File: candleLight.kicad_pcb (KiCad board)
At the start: 2 copper layers, 46.4 x 20 mm, 45 parts, among them J1 USB_C_Receptacle_USB2.0, J2 Conn_Phoenix, J3 Conn_SWD, J4 Conn_3.3V, U1 ME6210A33PG, U2 STM32F072C8Tx, U3 TJA1051/3, Y1 8MHz

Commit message: inital board
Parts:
- removed J4: Conn_3.3V, Connector_PinHeader_2.54mm:PinHeader_1x02_P2.54mm_Vertical
- removed R1, R2: 4K7, Resistor_SMD:R_0603_1608Metric
- removed SCL1: SCL1, Measurement_Points:Measurement_Point_Round-SMD-Pad_Small
- removed SDA1: SDA1, Measurement_Points:Measurement_Point_Round-SMD-Pad_Small
- removed W1, W2: TEST_1P, Measurement_Points:Measurement_Point_Round-SMD-Pad_Big
- removed W3, W4, W5, W6, W7, W8: TEST_1P, Measurement_Points:Measurement_Point_Round-SMD-Pad_Small
- added C13: 100nF, Capacitor_SMD:C_0603_1608Metric, F.Cu at (136.2, 77.0)
- added C14: 100nF, Capacitor_SMD:C_0603_1608Metric, F.Cu at (149.0, 71.0)
- added C15: 10uF, Capacitor_SMD:C_0805_2012Metric, F.Cu at (149.0, 69.0)
- added SW1: TS-1088R-02526, stm32world:TS-1088R-02526, F.Cu at (164.1, 88.0)
- added SW2: TS-1088R-02526, stm32world:TS-1088R-02526, F.Cu at (164.1, 84.0)
- added SW3: MST22D18G2 125, woldhack:SW-SMD_MST22D18G2, F.Cu at (130.4, 85.8)
- C1, C2: value 10uF -> 30pF; footprint Capacitor_SMD:C_0805_2012Metric -> Capacitor_SMD:C_0603_1608Metric
- C10: value 10uF -> 100nF; footprint Capacitor_SMD:C_0805_2012Metric -> Capacitor_SMD:C_0603_1608Metric
- C12, C5: value 100nF -> 10uF; footprint Capacitor_SMD:C_0603_1608Metric -> Capacitor_SMD:C_0805_2012Metric
- C3: value 30pF -> 100nF
- C4: value 30pF -> 10uF; footprint Capacitor_SMD:C_0603_1608Metric -> Capacitor_SMD:C_0805_2012Metric
- J3: value Conn_SWD -> Conn_01x05; footprint Connector_PinHeader_2.54mm:PinHeader_1x03_P2.54mm_Vertical -> Connector_PinHeader_2.54mm:PinHeader_1x05_P2.54mm_Vertical
- R11: value 5k1 -> 1K
- R3: value dnp -> 5k1; footprint Resistor_SMD:R_0805_2012Metric -> Resistor_SMD:R_0603_1608Metric
- R4: value 1K -> 5k1
- R5: value 5k1 -> 10K
- R7: value dnp -> 10K; footprint Resistor_SMD:R_0805_2012Metric -> Resistor_SMD:R_0603_1608Metric
- R8: value 1K -> 120
- U1: value ME6210A33PG -> STM32F072C8Tx; footprint Package_TO_SOT_SMD:SOT-89-3 -> Package_QFP:LQFP-48_7x7mm_P0.5mm
- U2: value STM32F072C8Tx -> ME6210A33PG; footprint Package_QFP:LQFP-48_7x7mm_P0.5mm -> Package_TO_SOT_SMD:SOT-89-3
- moved J1 125.0 mm to (168.8, 75.5), turned to 90 degrees
- moved J3 113.8 mm to (157.7, 65.0), turned to 90 degrees
- moved G*** 111.6 mm to (173.5, 43.5)
- moved R4 104.8 mm to (158.8, 73.8), turned to 180 degrees
- moved R5 103.6 mm to (152.6, 86.0)
- moved R3 102.4 mm to (158.8, 76.8), turned to 0 degrees
- moved U2 100.7 mm to (158.0, 85.5), turned to -90 degrees
- moved R11 96.7 mm to (143.9, 88.3)
- moved C4 94.2 mm to (158.9, 81.7), turned to 0 degrees
- moved R10 92.0 mm to (146.9, 88.3), turned to 90 degrees
- moved C7 89.6 mm to (138.5, 71.0)
- moved C5 89.6 mm to (154.4, 82.6), turned to 90 degrees
- moved D3 89.1 mm to (142.4, 88.3), turned to -90 degrees
- moved D2 88.9 mm to (145.4, 88.3), turned to -90 degrees
- moved C10 85.6 mm to (146.0, 81.8), turned to 180 degrees
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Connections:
- C1 pad 1: +5V -> GND
- C1 pad 2: GND -> Net-(U1-PF0)
- C11 pad 1: +5V -> +3V3
- C2 pad 1: +3V3 -> GND
- C2 pad 2: GND -> Net-(U1-PF1)
- C3 pad 1: GND -> NRST
- C3 pad 2: Net-(U2-PF0) -> GND
- C4 pad 1: GND -> +5V
- C4 pad 2: Net-(U2-PF1) -> GND
- C5 pad 1: NRST -> +3V3
- C6 pad 1: +3V3 -> +5V
- J3 pad 1: NRST -> +3V3
- J3 pad 2: SWCLK -> NRST
- J3 pad 3: SWDIO -> SWCLK
- R10 pad 1: Net-(D3-A) -> Net-(D2-A)
- R11 pad 1: Net-(J1-CC2) -> Net-(D3-A)
- R11 pad 2: GND -> +3V3
- R3 pad 1: +3V3 -> GND
- R3 pad 2: Net-(U2-BOOT0) -> Net-(J1-CC1)
- R4 pad 1: GND -> Net-(J1-CC2)
- R4 pad 2: Net-(U2-BOOT0) -> GND
- R5 pad 1: GND -> +3V3
- R5 pad 2: Net-(J1-CC1) -> NRST
- R7 pad 1: CAN_H -> BO0
- R7 pad 2: CAN_L -> GND
- R8 pad 1: Net-(D1-A) -> Net-(R8-Pad1)
- R8 pad 2: +3V3 -> CAN_L
- R9 pad 1: Net-(D2-A) -> Net-(D1-A)
- U1 pad 1: GND -> +3V3
- U1 pad 2: +5V -> CAN_S
- U1 pad 3: +3V3 -> unconnected-(U1-PC14-Pad3)
- U2 pad 1: +3V3 -> GND
- U2 pad 2: CAN_S -> +5V
- U2 pad 3: unconnected-(U2-PC14-Pad3) -> +3V3
- Y1 pad 1: Net-(U2-PF0) -> Net-(U1-PF0)
- Y1 pad 2: Net-(U2-PF1) -> Net-(U1-PF1)
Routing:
- net +3V3: track 7.37 -> 135.0 mm, vias 4 -> 8
- net NRST: track 20.2 -> 66.5 mm, vias 3 -> 4
- net BO0: track 0.00 -> 31.2 mm, vias 0 -> 3
- net GND: track 38.6 -> 10.8 mm
- net +5V: track 66.5 -> 52.8 mm, vias 5 -> 2
- net CAN_L: track 18.5 -> 30.9 mm
- net USB_DN: track 8.20 -> 20.1 mm
- net USB_DP: track 8.18 -> 20.1 mm
- net Net-(U1-PF0): track 0.00 -> 11.0 mm
- net CAN_H: track 20.2 -> 30.8 mm
- net Net-(U1-PF1): track 0.00 -> 9.83 mm
- net Net-(U2-PF1): track 9.24 -> 0.00 mm
- net Net-(U2-PB6): track 8.98 -> 0.00 mm, vias 1 -> 0
- net Net-(U2-PF0): track 8.31 -> 0.00 mm
- net Net-(U2-PB7): track 7.74 -> 0.00 mm, vias 1 -> 0
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- added copper zone on F.Cu, net GND
- removed copper zone on F.Cu, net +3V3
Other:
- board size 46.4 x 20 mm -> 59 x 29.6 mm
- board text removed: "+5V"
- board text removed: "3V3"
- board text removed: "B"
- board text removed: "CAN_H"
- board text removed: "CAN_L"
- board text removed: "CLK"
- board text removed: "CS"
- board text removed: "GND"
- board text removed: "IO"
- board text removed: "MISO"
- board text removed: "MOSI"
- board text removed: "PWR"
- board text removed: "RST"
- board text removed: "RX"
- board text removed: "SCK"
- board text removed: "SCL"
- board text removed: "SDA"
- board text removed: "T"
- board text removed: "TX"

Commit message: layout
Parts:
- removed C15: 10uF, Capacitor_SMD:C_0805_2012Metric
- removed R10, R11: 1K, Resistor_SMD:R_0603_1608Metric
- removed SW2: TS-1088R-02526, stm32world:TS-1088R-02526
- removed SW3: MST22D18G2 125, woldhack:SW-SMD_MST22D18G2
- added D4: PSM712, Package_TO_SOT_SMD:SOT-23, F.Cu at (158.5, 75.2)
- added D5: ~, Diode_SMD:D_SOD-123, F.Cu at (166.8, 82.5)
- added H1: MountingHole, MountingHole:MountingHole_2.1mm, F.Cu at (117.0, 63.8)
- added H2: MountingHole, MountingHole:MountingHole_2.1mm, F.Cu at (170.0, 63.8)
- added H3: MountingHole, MountingHole:MountingHole_2.1mm, F.Cu at (170.0, 87.2)
- added H4: MountingHole, MountingHole:MountingHole_2.1mm, F.Cu at (117.0, 87.2)
- added J4: Conn_USART1, Connector_PinHeader_2.54mm:PinHeader_1x02_P2.54mm_Vertical, F.Cu at (148.1, 87.3)
- added J5: Conn_BOOT0, Connector_PinHeader_2.54mm:PinHeader_1x03_P2.54mm_Vertical, F.Cu at (157.6, 63.7)
- added R1: 5k1, Resistor_SMD:R_0603_1608Metric, F.Cu at (160.8, 78.0)
- added R2: 5k1, Resistor_SMD:R_0603_1608Metric, F.Cu at (160.8, 72.8)
- C1, C2: value 30pF -> 20pF
- C11, C14: value 100nF -> 10uF; footprint Capacitor_SMD:C_0603_1608Metric -> Capacitor_SMD:C_0805_2012Metric
- C12: value 10uF -> 100nF; footprint Capacitor_SMD:C_0805_2012Metric -> Capacitor_SMD:C_0603_1608Metric
- C4, C5: value 10uF -> C_10UF_0805
- J3: value Conn_01x05 -> Conn_SWD
- R3, R4: value 5k1 -> 10K
- R6: value 10K -> 120
- R7: value 10K -> 1K
- R8: value 120 -> 1K
- SW1: value TS-1088R-02526 -> MST22D18G2 125; footprint stm32world:TS-1088R-02526 -> woldhack:SW-SMD_MST22D18G2
- U2: value ME6210A33PG -> AMS1117-3.3; footprint Package_TO_SOT_SMD:SOT-89-3 -> Package_TO_SOT_SMD:SOT-223-3_TabPin2
- U3: value TJA1051/3 -> TJA1051TK-3; footprint Package_SO:SOIC-8_3.9x4.9mm_P1.27mm -> Package_DFN_QFN:DFN-8-1EP_3x3mm_P0.65mm_EP1.55x2.4mm
- moved SW1 33.7 mm to (130.6, 84.6)
- moved R4 30.0 mm to (129.3, 67.9), turned to 0 degrees
- moved R7 21.0 mm to (136.6, 86.8), turned to 90 degrees
- moved R3 19.6 mm to (140.2, 83.0), turned to 180 degrees
- moved R8 18.9 mm to (141.2, 86.8), turned to 90 degrees
- moved R9 18.5 mm to (154.6, 77.6), turned to -90 degrees
- moved C11 16.8 mm to (146.0, 83.5), turned to 180 degrees
- moved R5 15.3 mm to (155.0, 70.9), turned to 180 degrees
- moved D3 15.1 mm to (153.1, 77.6), turned to 90 degrees
- moved C13 14.1 mm to (149.0, 71.0), turned to 0 degrees
- moved J3 13.9 mm to (143.9, 63.7)
- moved R6 11.9 mm to (126.3, 80.5), turned to 90 degrees
- moved C12 11.3 mm to (136.8, 77.0), turned to 90 degrees
- moved D2 5.94 mm to (139.7, 86.8)
- moved C4 4.49 mm to (163.2, 83.1), turned to -90 degrees
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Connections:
- J1 pad A4: +5V -> VBUS
- J1 pad A9: +5V -> VBUS
- J1 pad B4: +5V -> VBUS
- J1 pad B9: +5V -> VBUS
- J2 pad 1: CAN_L -> CAN_DN
- J2 pad 2: GND -> CAN_DP
- J2 pad 3: CAN_H -> GND
- R3 pad 1: GND -> +3V3
- R3 pad 2: Net-(J1-CC1) -> NRST
- R4 pad 1: Net-(J1-CC2) -> +3V3
- R4 pad 2: GND -> CAN_S
- R5 pad 1: +3V3 -> BO0
- R5 pad 2: NRST -> Net-(U1-BOOT0)
- R6 pad 1: +3V3 -> Net-(R6-Pad1)
- R6 pad 2: CAN_S -> CAN_DN
- R7 pad 1: BO0 -> Net-(D1-A)
- R7 pad 2: GND -> +3V3
- R8 pad 1: Net-(R8-Pad1) -> Net-(D2-A)
- R8 pad 2: CAN_L -> +3V3
- R9 pad 1: Net-(D1-A) -> Net-(D3-A)
- SW1 pad 1: GND -> unconnected-(SW1-Pad1)
- SW1 pad 2: NRST -> unconnected-(SW1-Pad2)
- U1 pad 30: unconnected-(U1-PA9-Pad30) -> USART1_TX
- U1 pad 31: unconnected-(U1-PA10-Pad31) -> USART1_RX
- U1 pad 44: BO0 -> Net-(U1-BOOT0)
- U2 pad 2: +5V -> +3V3
- U2 pad 3: +3V3 -> +5V
- U3 pad 6: CAN_L -> CAN_DN
- U3 pad 7: CAN_H -> CAN_DP
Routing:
- net NRST: track 66.5 -> 25.6 mm, vias 4 -> 2
- net CAN_L: track 30.9 -> 0.00 mm
- net CAN_H: track 30.8 -> 0.00 mm
- net CAN_DN: track 0.00 -> 30.5 mm
- net CAN_DP: track 0.00 -> 27.9 mm
- net BO0: track 31.2 -> 9.61 mm, vias 3 -> 0
- net Net-(U1-BOOT0): track 0.00 -> 14.5 mm, vias 0 -> 2
- net VBUS: track 0.00 -> 14.4 mm
- net USART1_RX: track 0.00 -> 14.0 mm
- net USART1_TX: track 0.00 -> 13.8 mm
- net SWCLK: track 21.0 -> 8.75 mm
- net SWDIO: track 21.5 -> 12.8 mm
- net LED2: track 16.7 -> 9.67 mm
- net +5V: track 52.8 -> 59.5 mm
- net +3V3: track 135.0 -> 141.2 mm, vias 8 -> 19
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- added copper zone on B.Cu, net +3V3
- added copper zone on F.Cu, net +3V3
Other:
- rule pad_to_mask_clearance: 0.05 -> 0

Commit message: update
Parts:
- moved G*** 13.3 mm to (161.2, 48.8)
- moved R6 1.62 mm to (126.5, 78.8)
- moved SW1 1.62 mm to (130.8, 83.0)
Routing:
- net CAN_DP: track 27.9 -> 28.6 mm
- net Net-(R6-Pad1): track 1.93 -> 1.33 mm
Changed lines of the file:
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@@
 	(footprint "woldhack:SW-SMD_MST22D18G2"
 		(layer "F.Cu")
-		(at 130.55 84.61 180)
+		(at 130.75 83 180)
 		(property "Reference" "SW1"
-			(at 5.46 -0.49 90)
+			(at 0 -4.75 180)
 			(layer "F.SilkS")
 			(effects
@@
 		(tags "THT Terminal Block Phoenix MKDS-1,5-3-5.08 pitch 5.08mm size 15.2x9.8mm drill 1.3mm pad 2.6mm")
 		(property "Reference" "J2"
-			(at 5.08 -6.32 90)
+			(at 2.33 -6.32 90)
 			(layer "F.SilkS")
 			(effects
@@
 	(footprint "Resistor_SMD:R_0603_1608Metric"
 		(layer "F.Cu")
-		(at 126.3 80.45 90)
+		(at 126.5 78.84 90)
 		(descr "Resistor SMD 0603 (1608 Metric), square (rectangular) end terminal, IPC-7351 nominal, (Body size source: IPC-SM-782 page 72, https://www.pcb-3d.com/wordpress/wp-content/uploads/ipc-sm-782a_amendment_1_and_2.pdf), generated with kicad-footprint-generator")
 		(tags "resistor")
 		(property "Reference" "R6"
-			(at 0.875 1.45 90)
+			(at 2.34 0 270)
 			(layer "F.SilkS")
 			(effects
@@
 	(footprint "LOGO"
 		(layer "B.Cu")
-		(at 173.5 43.5 90)
+		(at 161.25 48.75 90)
 		(property "Reference" "G***"
 			(at 0 0 90)
@@
 	)
 	(segment
-		(start 126.3 81.275)
-		(end 127.625 81.275)
+		(start 126.5 79.665)
+		(end 127.825 79.665)
 		(width 0.2)
 		(layer "F.Cu")
@@
 	)
 	(segment
-		(start 127.625 81.275)
-		(end 128.05 81.7)
-		(width 0.2286)
-		(layer "F.Cu")
-		(net 10)
-	)
-	(segment
 		(start 162.4 78)
 		(end 163.65 76.75)
@@
 	)
 	(segment
-		(start 130.55 81.7)
-		(end 130.55 80.94)
-		(width 0.2286)
+		(start 130.55 80.94)
+		(end 130.55 79.95)
+		(width 0.2)
+		(layer "F.Cu")
+		(net 37)
+	)
+	(segment
+		(start 130.55 79.95)
+		(end 123.295 72.695)
+		(width 0.2)
 		(layer "F.Cu")
 		(net 37)
@@
 	)
 	(segment
+		(start 130.55 80.35)
+		(end 130.55 80.94)
+		(width 0.2286)
+		(layer "F.Cu")
+		(net 37)
+	)
+	(segment
+		(start 123.295 72.695)
+		(end 122.305 72.695)
+		(width 0.2)
+		(layer "F.Cu")
+		(net 37)
+	)
+	(segment
 		(start 131.3775 66.985)
 		(end 130.889999 66.985)
@@
 	)
 	(segment
+		(start 130.75 80.15)
+		(end 130.55 80.35)
+		(width 0.2286)
+		(layer "F.Cu")
+		(net 37)
+	)
+	(segment
 		(start 130.789999 66.885)
 		(end 128.115 66.885)
@@
 	)
 	(segment
-		(start 130.55 80.94)
-		(end 122.305 72.695)
+		(start 117.51 72.46)
+		(end 117.51 76.29)
 		(width 0.2)
 		(layer "F.Cu")
-		(net 37)
+		(net 38)
 	)
 	(segment
@@
 	)
 	(segment
-		(start 119.05 77.83)
-		(end 124.505 77.83)
+		(start 119.235 78.015)
+		(end 126.5 78.015)
 		(width 0.2)
 		(layer "F.Cu")
@@
 	)
 	(segment
-		(start 117.51 72.46)
-		(end 117.51 76.29)
+		(start 117.51 76.29)
+		(end 119.235 78.015)
 		(width 0.2)
 		(layer "F.Cu")
@@
 	)
 	(segment
-		(start 124.505 77.83)
-		(end 126.3 79.625)
-		(width 0.2)
-		(layer "F.Cu")
-		(net 38)
-	)
-	(segment
 		(start 127.928603 66.435)
 		(end 123.943603 70.42)
 		(width 0.2)
 		(layer "F.Cu")
-		(net 38)
-	)
-	(segment
-		(start 117.51 76.29)
-		(end 119.05 77.83)
-		(width 0.2)
-		(layer "F.Cu")

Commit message: update silkscreen
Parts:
- moved G*** 33.4 mm to (141.3, 75.5), turned to -90 degrees
- moved R6 2.16 mm to (126.5, 81.0)
- moved SW1 1.75 mm to (130.8, 84.8)
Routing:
- net CAN_DP: track 28.6 -> 31.7 mm
- net CAN_DN: track 30.0 -> 31.3 mm
- net +3V3: track 141.2 -> 140.2 mm
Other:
- board text added: "3V3"
- board text added: "3v3"
- board text added: "BOOT0"
- board text added: "CLK"
- board text added: "DIO"
- board text added: "GND"
- board text added: "RST"
- board text added: "RX"
- board text added: "TX"

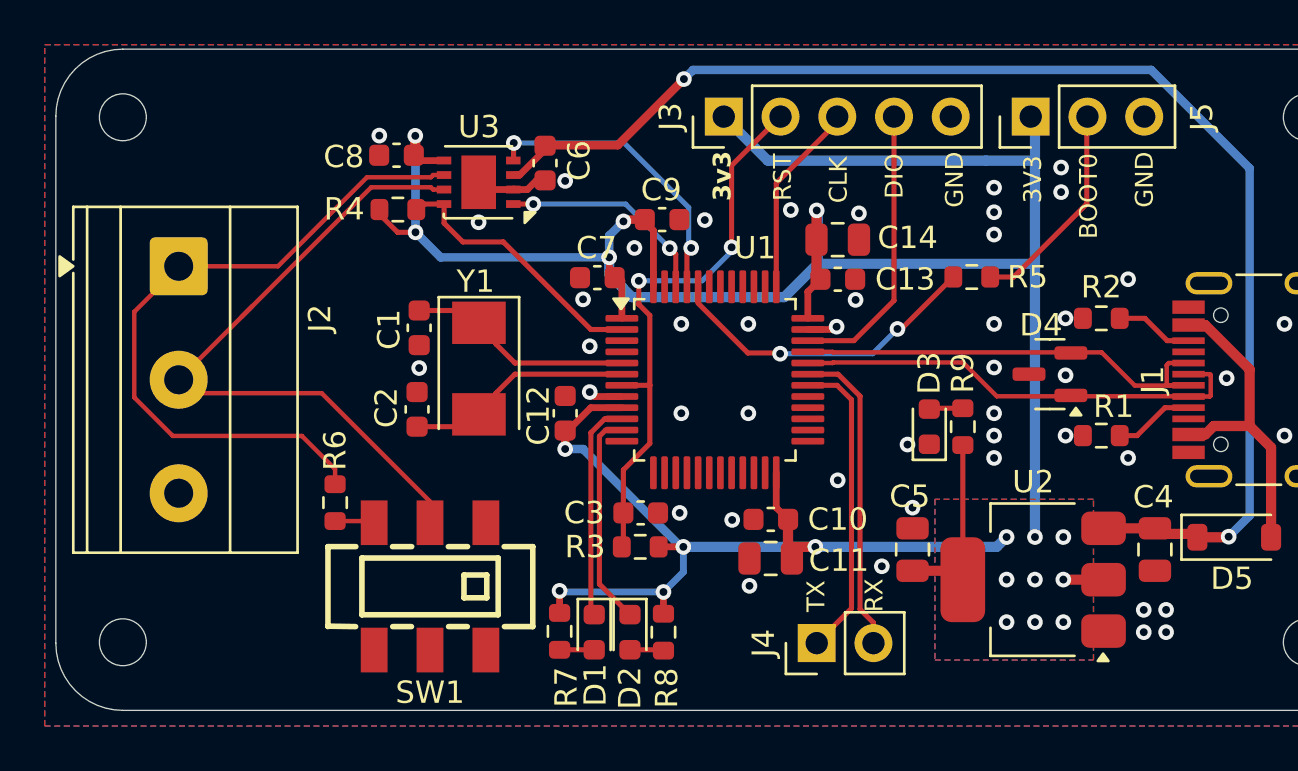
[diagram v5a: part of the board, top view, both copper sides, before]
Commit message: uppdate silkscreen and SPI header
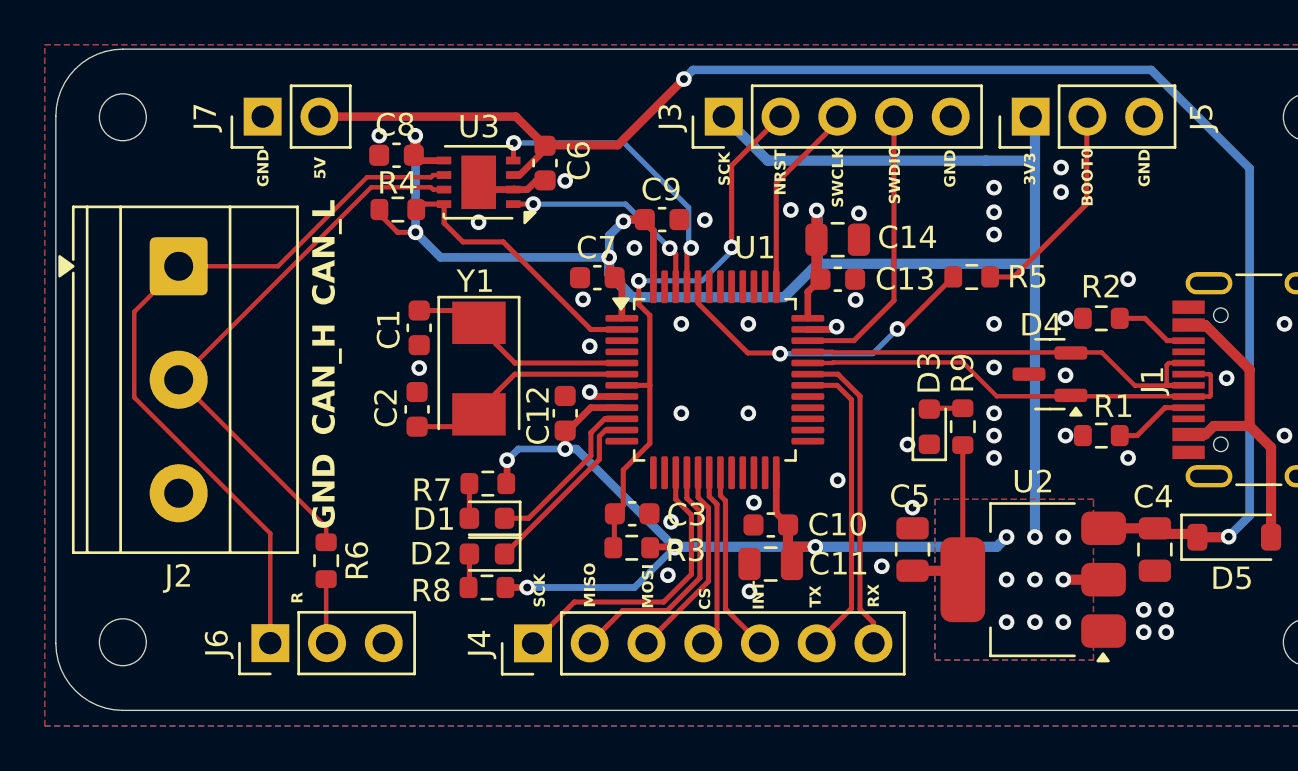
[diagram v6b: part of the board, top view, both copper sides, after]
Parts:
- removed SW1: MST22D18G2 125, woldhack:SW-SMD_MST22D18G2
- added J6: Conn_CAN_Jumper, Connector_PinHeader_2.54mm:PinHeader_1x03_P2.54mm_Vertical, F.Cu at (123.6, 87.3)
- added J7: Conn_5V, Connector_PinHeader_2.54mm:PinHeader_1x02_P2.54mm_Vertical, F.Cu at (123.3, 63.7)
- J4: value Conn_USART1 -> Conn_IO; footprint Connector_PinHeader_2.54mm:PinHeader_1x02_P2.54mm_Vertical -> Connector_PinHeader_2.54mm:PinHeader_1x07_P2.54mm_Vertical
- moved J4 12.7 mm to (135.4, 87.3)
- moved R8 8.15 mm to (133.3, 84.8), turned to 0 degrees
- moved R7 7.35 mm to (133.3, 80.2), turned to 0 degrees
- moved D2 7.29 mm to (133.3, 83.3), turned to 180 degrees
- moved D1 7.00 mm to (133.3, 81.7), turned to 180 degrees
- moved R6 2.63 mm to (126.1, 83.6)
- moved C3 0.38 mm to (139.8, 81.5)
- moved R3 0.38 mm to (139.8, 83.0)
- moved C10 0.25 mm to (146.0, 82.0)
- moved C11 0.25 mm to (146.0, 83.8)
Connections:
- J4 pad 1: USART1_TX -> SPI1_SCK
- J4 pad 2: USART1_RX -> SPI1_MISO
- R6 pad 2: CAN_DN -> CAN_DP
- U1 pad 15: unconnected-(U1-PA5-Pad15) -> SPI1_SCK
- U1 pad 16: unconnected-(U1-PA6-Pad16) -> SPI1_MISO
- U1 pad 17: unconnected-(U1-PA7-Pad17) -> SPI1_MOSI
- U1 pad 18: unconnected-(U1-PB0-Pad18) -> SPI_CS
- U1 pad 19: unconnected-(U1-PB1-Pad19) -> SPI_INT
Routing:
- net SPI1_SCK: track 0.00 -> 13.2 mm
- net SPI1_MISO: track 0.00 -> 11.1 mm
- net +5V: track 59.5 -> 70.1 mm
- net SPI1_MOSI: track 0.00 -> 8.98 mm
- net SPI_INT: track 0.00 -> 8.37 mm
- net SPI_CS: track 0.00 -> 8.04 mm
- net CAN_DP: track 31.7 -> 26.6 mm
- net +3V3: track 140.2 -> 143.4 mm
- net CAN_DN: track 31.3 -> 33.8 mm
- net LED1: track 9.85 -> 7.91 mm
- net LED2: track 9.67 -> 8.16 mm
- net Net-(J6-Pin_2): track 1.78 -> 2.88 mm
- net NRST: track 25.6 -> 26.1 mm
- net GND: vias 46 -> 47
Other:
- board text added: "5V"
- board text added: "CAN_H"
- board text added: "CAN_L"
- board text added: "CS"
- board text added: "INT"
- board text added: "MISO"
- board text added: "MOSI"
- board text added: "NRST"
- board text added: "R"
- board text added: "SCK"
- board text added: "SWCLK"
- board text added: "SWDIO"
- board text added: "candleLight V2.1"
- board text added: "woldhack 2025"
- board text removed: "3v3"
- board text removed: "CLK"
- board text removed: "DIO"
- board text removed: "RST"

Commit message: production
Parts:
- C4, C5: value C_10UF_0805 -> 10uF
